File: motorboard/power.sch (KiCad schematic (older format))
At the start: 28 parts, among them J3 Conn_01x02, J37 Screw_Terminal_01x02, Q3 PMV20ENR, U13 TPS2412PW, U3 TPS61093, U4 TPS63070

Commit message: Arduino is set up
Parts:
- added J?: Screw_Terminal_01x01, symbol Connector:Screw_Terminal_01x01
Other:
- moved on the sheet: D5
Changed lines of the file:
@@
 L Device:D_Schottky D5
 U 1 1 5DBE04C0
-P 1850 2950
-F 0 "D5" H 1850 2734 50  0000 C CNN
-F 1 "D_Schottky" H 1850 2825 50  0000 C CNN
-F 2 "Diode_SMD:D_SOD-123F" H 1850 2950 50  0001 C CNN
-F 3 "~" H 1850 2950 50  0001 C CNN
-	1    1850 2950
+P 1850 3300
+F 0 "D5" H 1850 3084 50  0000 C CNN
+F 1 "D_Schottky" H 1850 3175 50  0000 C CNN
+F 2 "Diode_SMD:D_SOD-123F" H 1850 3300 50  0001 C CNN
+F 3 "~" H 1850 3300 50  0001 C CNN
+	1    1850 3300
 	-1   0    0    1
 $EndComp
 Wire Wire Line
-	1150 2950 1700 2950
+	1150 3300 1700 3300
 $Comp
 L power:+BATT #PWR0101
@@
 L power:VBUS #PWR0106
 U 1 1 5DC1417D
-P 1150 2900
-F 0 "#PWR0106" H 1150 2750 50  0001 C CNN
-F 1 "VBUS" H 1165 3073 50  0000 C CNN
-F 2 "" H 1150 2900 50  0001 C CNN
-F 3 "" H 1150 2900 50  0001 C CNN
-	1    1150 2900
-	1    0    0    -1
-$EndComp
-Wire Wire Line
-	1150 2900 1150 2950
+P 1150 3250
+F 0 "#PWR0106" H 1150 3100 50  0001 C CNN
+F 1 "VBUS" H 1165 3423 50  0000 C CNN
+F 2 "" H 1150 3250 50  0001 C CNN
+F 3 "" H 1150 3250 50  0001 C CNN
+	1    1150 3250
+	1    0    0    -1
+$EndComp
+Wire Wire Line
+	1150 3250 1150 3300
 Wire Wire Line
 	2150 4450 2350 4450
@@
 	2350 4450 2350 4350
 Wire Wire Line
-	2000 2950 2350 2950
+	2000 3300 2350 3300
 $Comp
 L power:VDD #PWR0107
 U 1 1 5DC270AE
-P 2350 2900
-F 0 "#PWR0107" H 2350 2750 50  0001 C CNN
-F 1 "VDD" H 2367 3073 50  0000 C CNN
-F 2 "" H 2350 2900 50  0001 C CNN
-F 3 "" H 2350 2900 50  0001 C CNN
-	1    2350 2900
-	1    0    0    -1
-$EndComp
-Wire Wire Line
-	2350 2900 2350 2950
-Connection ~ 2350 2950
+P 2350 3250
+F 0 "#PWR0107" H 2350 3100 50  0001 C CNN
+F 1 "VDD" H 2367 3423 50  0000 C CNN
+F 2 "" H 2350 3250 50  0001 C CNN
+F 3 "" H 2350 3250 50  0001 C CNN
+	1    2350 3250
+	1    0    0    -1
+$EndComp
+Wire Wire Line
+	2350 3250 2350 3300
 Connection ~ 5300 5250
 Wire Wire Line
@@
 Wire Wire Line
 	2050 3800 2350 3800
-Connection ~ 2350 3800
 $Comp
 L power:+BATT #PWR0109
@@
 Wire Wire Line
 	4600 4750 4600 4700
-Wire Wire Line
-	2350 2950 2350 3800
+$Comp
+L Connector:Screw_Terminal_01x01 J?
+U 1 1 5E3B8F9F
+P 7750 4350
+F 0 "J?" H 7668 4125 50  0000 C CNN
+F 1 "Screw_Terminal_01x01" H 7668 4216 50  0000 C CNN
+F 2 "" H 7750 4350 50  0001 C CNN
+F 3 "~" H 7750 4350 50  0001 C CNN
+	1    7750 4350
+	-1   0    0    1
+$EndComp
+Wire Wire Line
+	2350 3300 2350 3800
+Connection ~ 2350 3300
+Connection ~ 2350 3800
 $EndSCHEMATC

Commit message: H-bridge setup complete
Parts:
- gave numbers to parts that had none: 1
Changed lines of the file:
@@
 $Descr A4 11693 8268
 encoding utf-8
-Sheet 2 3
+Sheet 2 2
 Title ""
 Date ""
@@
 	4600 4750 4600 4700
 $Comp
-L Connector:Screw_Terminal_01x01 J?
+L Connector:Screw_Terminal_01x01 J2
 U 1 1 5E3B8F9F
 P 7750 4350
-F 0 "J?" H 7668 4125 50  0000 C CNN
+F 0 "J2" H 7668 4125 50  0000 C CNN
 F 1 "Screw_Terminal_01x01" H 7668 4216 50  0000 C CNN
 F 2 "" H 7750 4350 50  0001 C CNN

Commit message: Complete - Rev1
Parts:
- removed C10, C7: 100n, Capacitor_SMD:C_0603_1608Metric, symbol Device:C
- removed C31: 10u, Capacitor_SMD:CP_Elec_4x5.4, symbol Device:C
- removed C6: 4u7, Capacitor_SMD:C_0603_1608Metric, symbol Device:C
- removed C8, C9: 1u, Capacitor_SMD:C_0603_1608Metric, symbol Device:C
- removed J2: Screw_Terminal_01x01, symbol Connector:Screw_Terminal_01x01
- removed J3: Conn_01x02, Connector_JST:JST_PH_S2B-PH-K_1x02_P2.00mm_Horizontal, symbol Connector_Generic:Conn_01x02
- removed J37: Screw_Terminal_01x02, TerminalBlock_Phoenix:TerminalBlock_Phoenix_MPT-2.54mm_2pol, symbol Connector:Screw_Terminal_01x02
- removed L1: 10u, Inductor_SMD:L_Taiyo-Yuden_NR-30xx, symbol pspice:INDUCTOR
- removed R16: 191k, Resistor_SMD:R_0603_1608Metric, symbol Device:R_Small
- removed R17: 10k, Resistor_SMD:R_0603_1608Metric, symbol Device:R_Small
- removed R18: 200k, Resistor_SMD:R_0603_1608Metric, symbol Device:R
- removed U3: TPS61093, Housings_SON:Texas_S-PWSON-N10_ThermalVias, symbol daq-hardware-rescue:TPS61093-iclr
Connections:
- net labels added: +15V
- net labels removed: +10V, +5V, +BATT, VO
- wire segments 118 -> 65
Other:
- note added: "Powa!!"
- moved on the sheet: C11, C28, C29, C30, C4, C5, D5, L3, Q3, R19, R21, R23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

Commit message: nearrrly there
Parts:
- added D?: D_Schottky, Diode_SMD:D_SOD-123F, symbol Device:D_Schottky
- added J?: Separate LiPo, symbol Connector:Conn_01x02_Male
- added JP?: Jumper, symbol Jumper:SolderJumper_3_Open
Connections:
- net GND: now also J?.2 (Pin_2)
- net VDD: now also D?.1 (K)
- new net: D?.2 (A), J?.1 (Pin_1)
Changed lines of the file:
@@
 encoding utf-8
 Sheet 2 3
-Title ""
-Date ""
-Rev ""
-Comp ""
+Title "Power"
+Date "2020-02-12"
+Rev "2"
+Comp "Raihaan Usman"
 Comment1 ""
 Comment2 ""
@@
 Text Notes 4700 2150 0    303  ~ 61
 Powa!!
+$Comp
+L Jumper:SolderJumper_3_Open JP?
+U 1 1 5E8D85AC
+P 3850 7000
+F 0 "JP?" V 3896 7067 50  0000 L CNN
+F 1 "Jumper" V 3805 7067 50  0000 L CNN
+F 2 "" H 3850 7000 50  0001 C CNN
+F 3 "~" H 3850 7000 50  0001 C CNN
+	1    3850 7000
+	0    -1   -1   0
+$EndComp
+$Comp
+L Connector:Conn_01x02_Male J?
+U 1 1 5E8D9BD5
+P 1650 6800
+F 0 "J?" H 1700 6900 50  0000 C CNN
+F 1 "Separate LiPo" V 1550 6750 50  0000 C CNN
+F 2 "" H 1650 6800 50  0001 C CNN
+F 3 "~" H 1650 6800 50  0001 C CNN
+	1    1650 6800
+	1    0    0    -1
+$EndComp
+Wire Wire Line
+	1850 6800 2050 6800
+Wire Wire Line
+	1850 6900 1950 6900
+Wire Wire Line
+	1950 6900 1950 7000
+$Comp
+L power:GND #PWR?
+U 1 1 5E8DC9A0
+P 1950 7000
+F 0 "#PWR?" H 1950 6750 50  0001 C CNN
+F 1 "GND" H 1955 6827 50  0000 C CNN
+F 2 "" H 1950 7000 50  0001 C CNN
+F 3 "" H 1950 7000 50  0001 C CNN
+	1    1950 7000
+	1    0    0    -1
+$EndComp
+$Comp
+L Device:D_Schottky D?
+U 1 1 5E8DDA00
+P 2200 6800
+F 0 "D?" H 2200 6584 50  0000 C CNN
+F 1 "D_Schottky" H 2200 6675 50  0000 C CNN
+F 2 "Diode_SMD:D_SOD-123F" H 2200 6800 50  0001 C CNN
+F 3 "~" H 2200 6800 50  0001 C CNN
+	1    2200 6800
+	-1   0    0    1
+$EndComp
+Wire Wire Line
+	2350 6800 2550 6800
+$Comp
+L power:VDD #PWR?
+U 1 1 5E8E20B4
+P 2550 6800
+F 0 "#PWR?" H 2550 6650 50  0001 C CNN
+F 1 "VDD" H 2567 6973 50  0000 C CNN
+F 2 "" H 2550 6800 50  0001 C CNN
+F 3 "" H 2550 6800 50  0001 C CNN
+	1    2550 6800
+	1    0    0    -1
+$EndComp
 $EndSCHEMATC

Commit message: neater
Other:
- moved on the sheet: JP?
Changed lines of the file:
@@
 L Jumper:SolderJumper_3_Open JP?
 U 1 1 5E8D85AC
-P 3850 7000
-F 0 "JP?" V 3896 7067 50  0000 L CNN
-F 1 "Jumper" V 3805 7067 50  0000 L CNN
-F 2 "" H 3850 7000 50  0001 C CNN
-F 3 "~" H 3850 7000 50  0001 C CNN
-	1    3850 7000
+P 3950 7000
+F 0 "JP?" V 3996 7067 50  0000 L CNN
+F 1 "Jumper" V 3905 7067 50  0000 L CNN
+F 2 "" H 3950 7000 50  0001 C CNN
+F 3 "~" H 3950 7000 50  0001 C CNN
+	1    3950 7000
 	0    -1   -1   0
 $EndComp

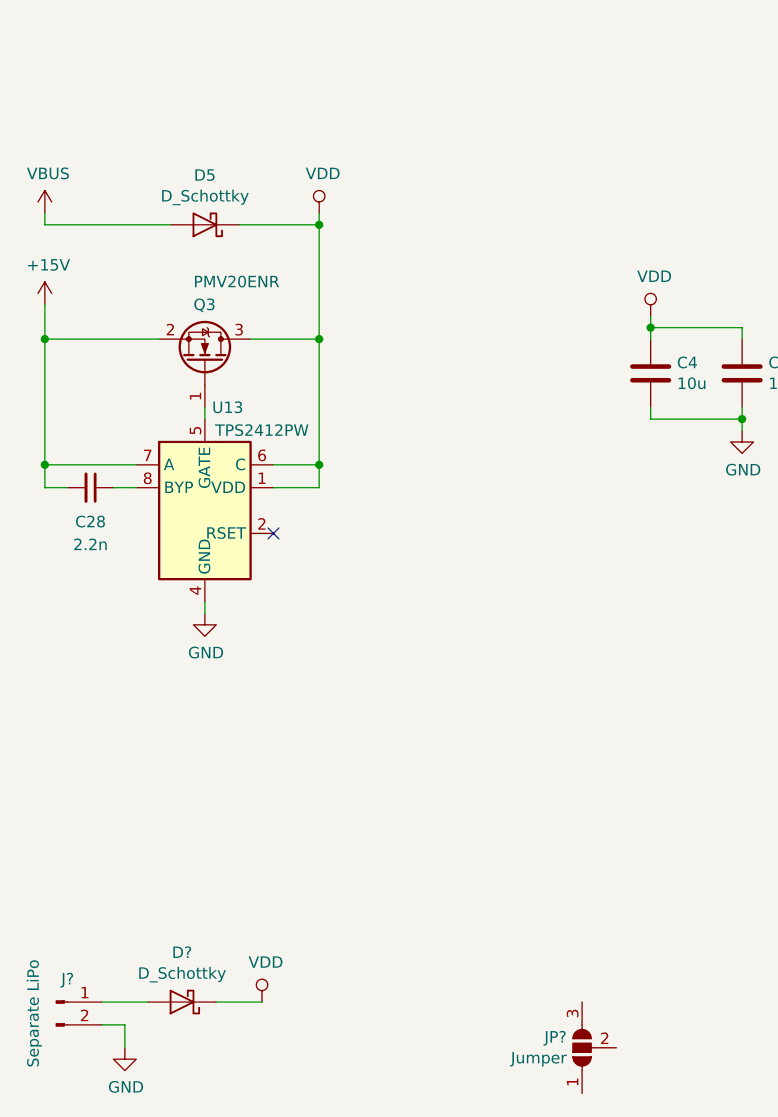
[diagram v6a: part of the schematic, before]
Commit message: Debugged
*Should* work
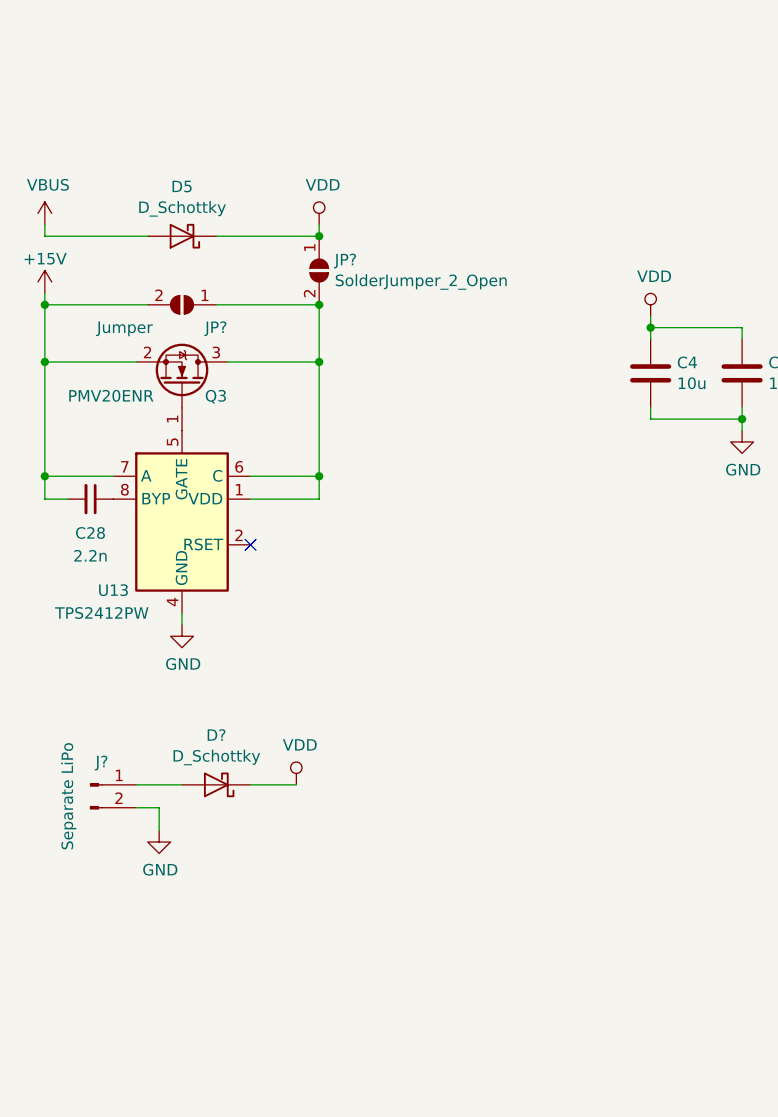
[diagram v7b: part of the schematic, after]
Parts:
- removed JP?: Jumper, symbol Jumper:SolderJumper_3_Open
- added JP?: SolderJumper_2_Open, symbol Jumper:SolderJumper_2_Open
- added JP?: Jumper, symbol Jumper:SolderJumper_2_Open
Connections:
- net +15V: now also JP?.2 (B)
- net VDD: now also JP?.1 (A); no longer Q3.3 (D), U13.1 (VDD), U13.6 (C)
- new net: JP?.1 (A), JP?.2 (B), Q3.3 (D), U13.1 (VDD), U13.6 (C)
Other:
- moved on the sheet: C28, D5, D?, J?, Q3, U13
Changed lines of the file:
@@
 L daq-hardware-rescue:TPS2412PW-Power_Management U13
 U 1 1 5DBCF369
-P 2300 4650
+P 2200 4700
 AR Path="/5DBCF369" Ref="U13"  Part="1"
 AR Path="/5DAD2180/5DBCF369" Ref="U13"  Part="1"
-F 0 "U13" H 2400 5100 50  0000 C CNN
-F 1 "TPS2412PW" H 2550 5000 50  0000 C CNN
-F 2 "Package_SO:TSSOP-8_4.4x3mm_P0.65mm" H 4400 4450 50  0001 C CNN
-F 3 "http://www.ti.com/lit/ds/symlink/tps2412.pdf" H 4400 4450 50  0001 C CNN
-	1    2300 4650
+F 0 "U13" H 1900 4400 50  0000 C CNN
+F 1 "TPS2412PW" H 1850 4300 50  0000 C CNN
+F 2 "Package_SO:TSSOP-8_4.4x3mm_P0.65mm" H 4300 4500 50  0001 C CNN
+F 3 "http://www.ti.com/lit/ds/symlink/tps2412.pdf" H 4300 4500 50  0001 C CNN
+	1    2200 4700
 	1    0    0    -1
 $EndComp
@@
 L Device:D_Schottky D5
 U 1 1 5DBE04C0
-P 2300 3400
-F 0 "D5" H 2300 3184 50  0000 C CNN
-F 1 "D_Schottky" H 2300 3275 50  0000 C CNN
-F 2 "Diode_SMD:D_SOD-123F" H 2300 3400 50  0001 C CNN
-F 3 "~" H 2300 3400 50  0001 C CNN
-	1    2300 3400
+P 2200 3450
+F 0 "D5" H 2200 3234 50  0000 C CNN
+F 1 "D_Schottky" H 2200 3325 50  0000 C CNN
+F 2 "Diode_SMD:D_SOD-123F" H 2200 3450 50  0001 C CNN
+F 3 "~" H 2200 3450 50  0001 C CNN
+	1    2200 3450
 	-1   0    0    1
 $EndComp
-Wire Wire Line
-	1600 3400 2150 3400
 $Comp
 L power:VBUS #PWR0106
 U 1 1 5DC1417D
-P 1600 3350
-F 0 "#PWR0106" H 1600 3200 50  0001 C CNN
-F 1 "VBUS" H 1615 3523 50  0000 C CNN
-F 2 "" H 1600 3350 50  0001 C CNN
-F 3 "" H 1600 3350 50  0001 C CNN
-	1    1600 3350
-	1    0    0    -1
-$EndComp
-Wire Wire Line
-	1600 3350 1600 3400
-Wire Wire Line
-	2600 4550 2800 4550
-Wire Wire Line
-	2800 4550 2800 4450
-Wire Wire Line
-	2450 3400 2800 3400
+P 1600 3400
+F 0 "#PWR0106" H 1600 3250 50  0001 C CNN
+F 1 "VBUS" H 1615 3573 50  0000 C CNN
+F 2 "" H 1600 3400 50  0001 C CNN
+F 3 "" H 1600 3400 50  0001 C CNN
+	1    1600 3400
+	1    0    0    -1
+$EndComp
+Wire Wire Line
+	1600 3400 1600 3450
 $Comp
 L power:VDD #PWR0107
 U 1 1 5DC270AE
-P 2800 3350
-F 0 "#PWR0107" H 2800 3200 50  0001 C CNN
-F 1 "VDD" H 2817 3523 50  0000 C CNN
-F 2 "" H 2800 3350 50  0001 C CNN
-F 3 "" H 2800 3350 50  0001 C CNN
-	1    2800 3350
-	1    0    0    -1
-$EndComp
-Wire Wire Line
-	2800 3350 2800 3400
+P 2800 3400
+F 0 "#PWR0107" H 2800 3250 50  0001 C CNN
+F 1 "VDD" H 2817 3573 50  0000 C CNN
+F 2 "" H 2800 3400 50  0001 C CNN
+F 3 "" H 2800 3400 50  0001 C CNN
+	1    2800 3400
+	1    0    0    -1
+$EndComp
+Wire Wire Line
+	2800 3400 2800 3450
 $Comp
 L power:GND #PWR0108
 U 1 1 5DC2CCED
-P 2300 5100
-F 0 "#PWR0108" H 2300 4850 50  0001 C CNN
-F 1 "GND" H 2305 4927 50  0000 C CNN
-F 2 "" H 2300 5100 50  0001 C CNN
-F 3 "" H 2300 5100 50  0001 C CNN
-	1    2300 5100
-	1    0    0    -1
-$EndComp
-Wire Wire Line
-	2300 5100 2300 5050
+P 2200 5150
+F 0 "#PWR0108" H 2200 4900 50  0001 C CNN
+F 1 "GND" H 2205 4977 50  0000 C CNN
+F 2 "" H 2200 5150 50  0001 C CNN
+F 3 "" H 2200 5150 50  0001 C CNN
+	1    2200 5150
+	1    0    0    -1
+$EndComp
+Wire Wire Line
+	2200 5150 2200 5100
 $Comp
 L Device:Q_NMOS_GSD Q?
 U 1 1 5DC402F2
-P 2300 4000
+P 2200 4100
 AR Path="/5DB4FA2A/5DC402F2" Ref="Q?"  Part="1"
 AR Path="/5DAD2180/5DC402F2" Ref="Q3"  Part="1"
-F 0 "Q3" V 2550 3950 50  0000 L CNN
-F 1 "PMV20ENR" V 2650 3950 50  0000 L CNN
-F 2 "Package_TO_SOT_SMD:SOT-23" H 2500 4100 50  0001 C CNN
-F 3 "~" H 2300 4000 50  0001 C CNN
-	1    2300 4000
+F 0 "Q3" V 2150 4200 50  0000 L CNN
+F 1 "PMV20ENR" V 2150 3600 50  0000 L CNN
+F 2 "Package_TO_SOT_SMD:SOT-23" H 2400 4200 50  0001 C CNN
+F 3 "~" H 2200 4100 50  0001 C CNN
+	1    2200 4100
 	0    1    -1   0
 $EndComp
-Wire Wire Line
-	2300 4200 2300 4250
-Wire Wire Line
-	2600 4450 2800 4450
-Connection ~ 2800 4450
-Wire Wire Line
-	2800 4450 2800 3900
-Wire Wire Line
-	2500 3900 2800 3900
-Wire Wire Line
-	1600 3750 1600 3900
-Wire Wire Line
-	1600 3900 2100 3900
-Wire Wire Line
-	1600 3900 1600 4450
-Connection ~ 1600 3900
 $Comp
 L Device:C_Small C28
 U 1 1 5DC81713
-P 1800 4550
-F 0 "C28" V 1950 4550 50  0000 C CNN
-F 1 "2.2n" V 2050 4550 50  0000 C CNN
-F 2 "Capacitor_SMD:C_0603_1608Metric" H 1800 4550 50  0001 C CNN
-F 3 "~" H 1800 4550 50  0001 C CNN
-	1    1800 4550
+P 1800 4600
+F 0 "C28" V 1950 4600 50  0000 C CNN
+F 1 "2.2n" V 2050 4600 50  0000 C CNN
+F 2 "Capacitor_SMD:C_0603_1608Metric" H 1800 4600 50  0001 C CNN
+F 3 "~" H 1800 4600 50  0001 C CNN
+	1    1800 4600
 	0    1    1    0
 $EndComp
 Wire Wire Line
-	1600 4450 2000 4450
-Wire Wire Line
-	1900 4550 2000 4550
-Wire Wire Line
-	1700 4550 1600 4550
-Wire Wire Line
-	1600 4550 1600 4450
-Connection ~ 1600 4450
-NoConn ~ 2600 4750
+	1700 4600 1600 4600
 $Comp
 L daq-hardware-rescue:TPS63070-iclr U4
@@
 Text Label 9600 3900 2    50   ~ 0
 FB_3V3
-Wire Wire Line
-	2800 3400 2800 3900
-Connection ~ 2800 3400
-Connection ~ 2800 3900
 $Comp
 L power:+15V #PWR?
 U 1 1 5E621E3E
-P 1600 3750
-F 0 "#PWR?" H 1600 3600 50  0001 C CNN
-F 1 "+15V" H 1615 3923 50  0000 C CNN
-F 2 "" H 1600 3750 50  0001 C CNN
-F 3 "" H 1600 3750 50  0001 C CNN
-	1    1600 3750
+P 1600 3700
+F 0 "#PWR?" H 1600 3550 50  0001 C CNN
+F 1 "+15V" H 1600 3850 50  0000 C CNN
+F 2 "" H 1600 3700 50  0001 C CNN
+F 3 "" H 1600 3700 50  0001 C CNN
+	1    1600 3700
 	1    0    0    -1
 $EndComp
@@
 Powa!!
 $Comp
-L Jumper:SolderJumper_3_Open JP?
-U 1 1 5E8D85AC
-P 3950 7000
-F 0 "JP?" V 3996 7067 50  0000 L CNN
-F 1 "Jumper" V 3905 7067 50  0000 L CNN
-F 2 "" H 3950 7000 50  0001 C CNN
-F 3 "~" H 3950 7000 50  0001 C CNN
-	1    3950 7000
-	0    -1   -1   0
-$EndComp
-$Comp
 L Connector:Conn_01x02_Male J?
 U 1 1 5E8D9BD5
-P 1650 6800
-F 0 "J?" H 1700 6900 50  0000 C CNN
-F 1 "Separate LiPo" V 1550 6750 50  0000 C CNN
-F 2 "" H 1650 6800 50  0001 C CNN
-F 3 "~" H 1650 6800 50  0001 C CNN
-	1    1650 6800
-	1    0    0    -1
-$EndComp
-Wire Wire Line
-	1850 6800 2050 6800
-Wire Wire Line
-	1850 6900 1950 6900
-Wire Wire Line
-	1950 6900 1950 7000
+P 1800 5850
+F 0 "J?" H 1850 5950 50  0000 C CNN
+F 1 "Separate LiPo" V 1700 5800 50  0000 C CNN
+F 2 "" H 1800 5850 50  0001 C CNN
+F 3 "~" H 1800 5850 50  0001 C CNN
+	1    1800 5850
+	1    0    0    -1
+$EndComp
+Wire Wire Line
+	2000 5950 2100 5950
+Wire Wire Line
+	2100 5950 2100 6050
 $Comp
 L power:GND #PWR?
 U 1 1 5E8DC9A0
-P 1950 7000
-F 0 "#PWR?" H 1950 6750 50  0001 C CNN
-F 1 "GND" H 1955 6827 50  0000 C CNN
-F 2 "" H 1950 7000 50  0001 C CNN
-F 3 "" H 1950 7000 50  0001 C CNN
-	1    1950 7000
-	1    0    0    -1
-$EndComp
+P 2100 6050
+F 0 "#PWR?" H 2100 5800 50  0001 C CNN
+F 1 "GND" H 2105 5877 50  0000 C CNN
+F 2 "" H 2100 6050 50  0001 C CNN
+F 3 "" H 2100 6050 50  0001 C CNN
+	1    2100 6050
+	1    0    0    -1
+$EndComp
+$Comp
+L power:VDD #PWR?
+U 1 1 5E8E20B4
+P 2700 5850
+F 0 "#PWR?" H 2700 5700 50  0001 C CNN
+F 1 "VDD" H 2717 6023 50  0000 C CNN
+F 2 "" H 2700 5850 50  0001 C CNN
+F 3 "" H 2700 5850 50  0001 C CNN
+	1    2700 5850
+	1    0    0    -1
+$EndComp
+$Comp
+L Jumper:SolderJumper_2_Open JP?
+U 1 1 5E471230
+P 2800 3600
+F 0 "JP?" V 2754 3668 50  0000 L CNN
+F 1 "SolderJumper_2_Open" V 2845 3668 50  0000 L CNN
+F 2 "" H 2800 3600 50  0001 C CNN
+F 3 "~" H 2800 3600 50  0001 C CNN
+	1    2800 3600
+	0    1    1    0
+$EndComp
+$Comp
+L Jumper:SolderJumper_2_Open JP?
+U 1 1 5E47891E
+P 2200 3750
+F 0 "JP?" H 2050 3850 50  0000 C CNN
+F 1 "Jumper" H 2450 3850 50  0000 C CNN
+F 2 "" H 2200 3750 50  0001 C CNN
+F 3 "~" H 2200 3750 50  0001 C CNN
+	1    2200 3750
+	-1   0    0    1
+$EndComp
+Wire Wire Line
+	2000 5850 2200 5850
+Wire Wire Line
+	2500 5850 2700 5850
 $Comp
 L Device:D_Schottky D?
 U 1 1 5E8DDA00
-P 2200 6800
-F 0 "D?" H 2200 6584 50  0000 C CNN
-F 1 "D_Schottky" H 2200 6675 50  0000 C CNN
-F 2 "Diode_SMD:D_SOD-123F" H 2200 6800 50  0001 C CNN
-F 3 "~" H 2200 6800 50  0001 C CNN
-	1    2200 6800
+P 2350 5850
+F 0 "D?" H 2350 5634 50  0000 C CNN
+F 1 "D_Schottky" H 2350 5725 50  0000 C CNN
+F 2 "Diode_SMD:D_SOD-123F" H 2350 5850 50  0001 C CNN
+F 3 "~" H 2350 5850 50  0001 C CNN
+	1    2350 5850
 	-1   0    0    1
 $EndComp
 Wire Wire Line
-	2350 6800 2550 6800
-$Comp
-L power:VDD #PWR?
-U 1 1 5E8E20B4
-P 2550 6800
-F 0 "#PWR?" H 2550 6650 50  0001 C CNN
-F 1 "VDD" H 2567 6973 50  0000 C CNN
-F 2 "" H 2550 6800 50  0001 C CNN
-F 3 "" H 2550 6800 50  0001 C CNN
-	1    2550 6800
-	1    0    0    -1
-$EndComp
+	1600 3750 1600 4000
+NoConn ~ 2500 4800
+Wire Wire Line
+	2500 4600 2800 4600
+Wire Wire Line
+	2800 4600 2800 4500
+Wire Wire Line
+	2500 4500 2800 4500
+Connection ~ 2800 4500
+Wire Wire Line
+	2000 4000 1600 4000
+Connection ~ 1600 4000
+Wire Wire Line
+	1600 4000 1600 4500
+Wire Wire Line
+	1900 4500 1600 4500
+Connection ~ 1600 4500
+Wire Wire Line
+	1600 4500 1600 4600
+Wire Wire Line
+	2400 4000 2800 4000
+Wire Wire Line
+	2800 4000 2800 4500
+Wire Wire Line
+	2800 4000 2800 3750
+Connection ~ 2800 4000
+Connection ~ 2800 3750
+Wire Wire Line
+	2350 3750 2800 3750
+Wire Wire Line
+	2050 3750 1600 3750
+Connection ~ 1600 3750
+Wire Wire Line
+	1600 3750 1600 3700
+Wire Wire Line
+	1600 3450 2050 3450
+Wire Wire Line
+	2350 3450 2800 3450
+Connection ~ 2800 3450
 $EndSCHEMATC

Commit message: PCB build started
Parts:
- C11: renamed from C29; footprint Capacitor_SMD:CP_Elec_4x5.4 -> Capacitor_SMD:C_0603_1608Metric
- C12: renamed from C30; footprint Capacitor_SMD:CP_Elec_4x5.4 -> Capacitor_SMD:C_0603_1608Metric
- C8: renamed from C4; footprint Capacitor_SMD:CP_Elec_4x5.4 -> Capacitor_SMD:C_0603_1608Metric
- C9: renamed from C5; footprint Capacitor_SMD:CP_Elec_4x5.4 -> Capacitor_SMD:C_0603_1608Metric
- J8: renamed from J?; footprint (none) -> Connector_PinHeader_2.54mm:PinHeader_1x02_P2.54mm_Vertical
- JP4: renamed from JP?; value Jumper -> Jumper1; footprint (none) -> Jumper:SolderJumper-2_P1.3mm_Open_RoundedPad1.0x1.5mm
- JP5: renamed from JP?; value SolderJumper_2_Open -> Jumper2; footprint (none) -> Jumper:SolderJumper-2_P1.3mm_Open_RoundedPad1.0x1.5mm
- gave numbers to parts that had none: 1
- renumbered C11 to C10, C28 to C7, D5 to D3, L3 to L1, Q3 to Q1, R23 to R10, R24 to R11, R19 to R8, R21 to R9, U13 to U3
